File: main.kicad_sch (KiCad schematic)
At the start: 85 parts, among them J1 USB_C_Receptacle, J2 SPIheader, J3 Bus_PCI_Express_x4, U2 SPI_SOIC-8, U3 SPI_DFN-8, Y1 25MHz

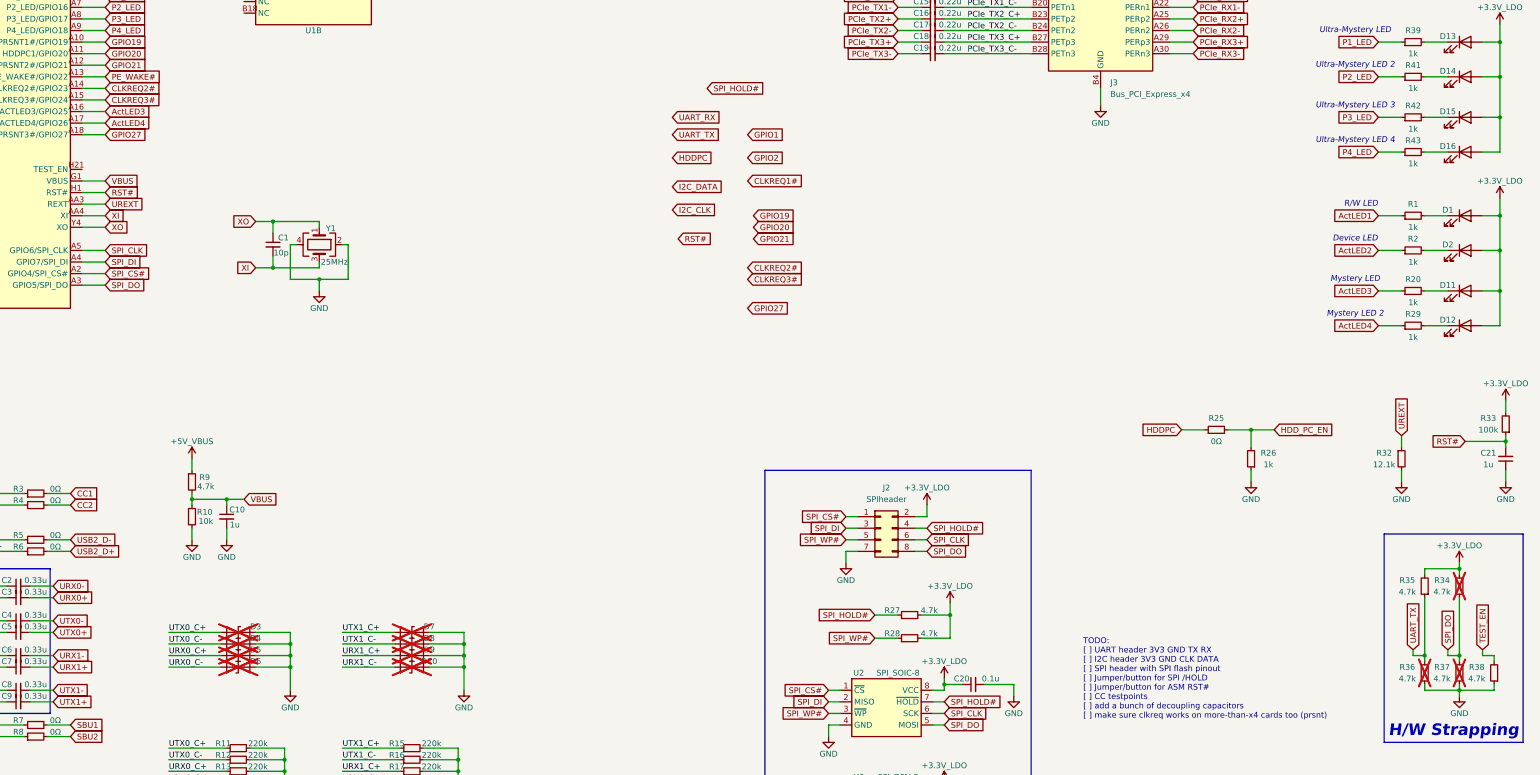
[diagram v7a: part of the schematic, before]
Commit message: Very bad routing lol
should probably not try to make it *that* compact
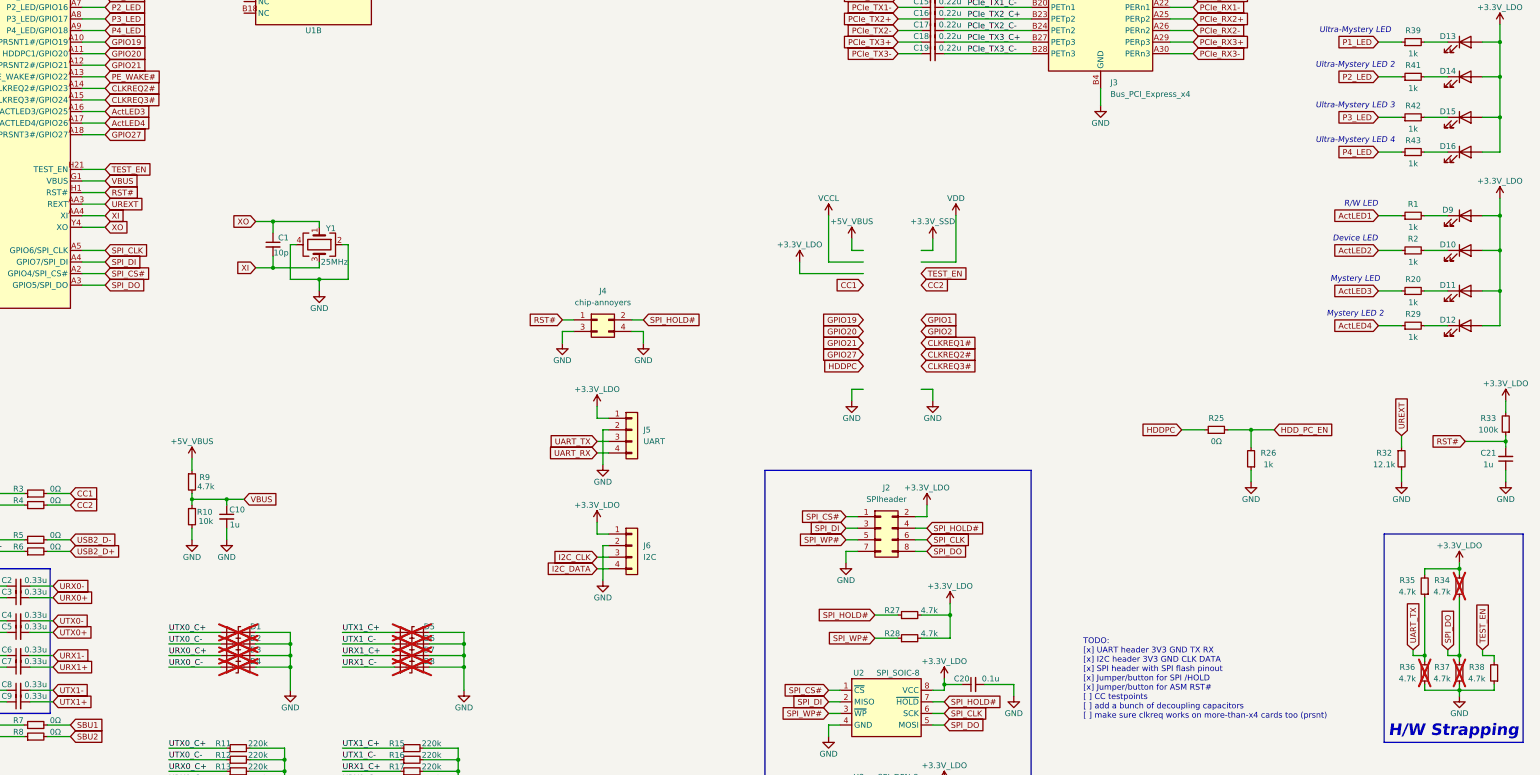
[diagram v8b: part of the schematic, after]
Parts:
- added J4: chip-annoyers, Connector_PinHeader_2.54mm:PinHeader_2x02_P2.54mm_Vertical, symbol Connector_Generic:Conn_02x02_Odd_Even
- added J5: UART, Connector_PinHeader_2.54mm:PinHeader_1x04_P2.54mm_Vertical, symbol Connector_Generic:Conn_01x04
- added J6: I2C, Connector_PinHeader_2.54mm:PinHeader_1x04_P2.54mm_Vertical, symbol Connector_Generic:Conn_01x04
- renumbered D3 to D1, D2 to D10, D4 to D2, D5 to D3, D6 to D4, D7 to D5, D8 to D6, D9 to D7, D10 to D8, D1 to D9
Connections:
- net +3.3V_LDO: now also J5.1 (Pin_1), J6.1 (Pin_1)
- net GND: now also J4.3 (Pin_3), J4.4 (Pin_4), J5.2 (Pin_2), J6.2 (Pin_2)
- net I2C_CLK: now also J6.3 (Pin_3)
- net I2C_DATA: now also J6.4 (Pin_4)
- net RST#: now also J4.1 (Pin_1)
- net SPI_HOLD#: now also J4.2 (Pin_2)
- net TEST_EN: now also U1.H21 (TEST_EN)
- net UART_RX: now also J5.4 (Pin_4)
- net UART_TX: now also J5.3 (Pin_3)
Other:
- note added: "TODO: [x] UART header 3V3 GND TX RX [x] I2C header 3V3 GND CLK DATA [x] SPI header with SPI flash pinout [x] Jumper/button for SPI /HOLD [x] Jumper/button for ASM RST# [ ] CC testpoints [ ] add a bunch of decoupling capacitors [ ] make sure clkreq works on more-than-x4 cards too (prsnt)"
- note removed: "TODO: [ ] UART header 3V3 GND TX RX [ ] I2C header 3V3 GND CLK DATA [ ] SPI header with SPI flash pinout [ ] Jumper/button for SPI /HOLD [ ] Jumper/button for ASM RST# [ ] CC testpoints [ ] add a bunch of decoupling capacitors [ ] make sure clkreq works on more-than-x4 cards too (prsnt)"
